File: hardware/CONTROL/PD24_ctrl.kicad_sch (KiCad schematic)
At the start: 11 parts, among them J1 Conn_01x12_Socket, J2 Conn_01x08_Socket, U2 STM32G031G8Ux, U5 INA228

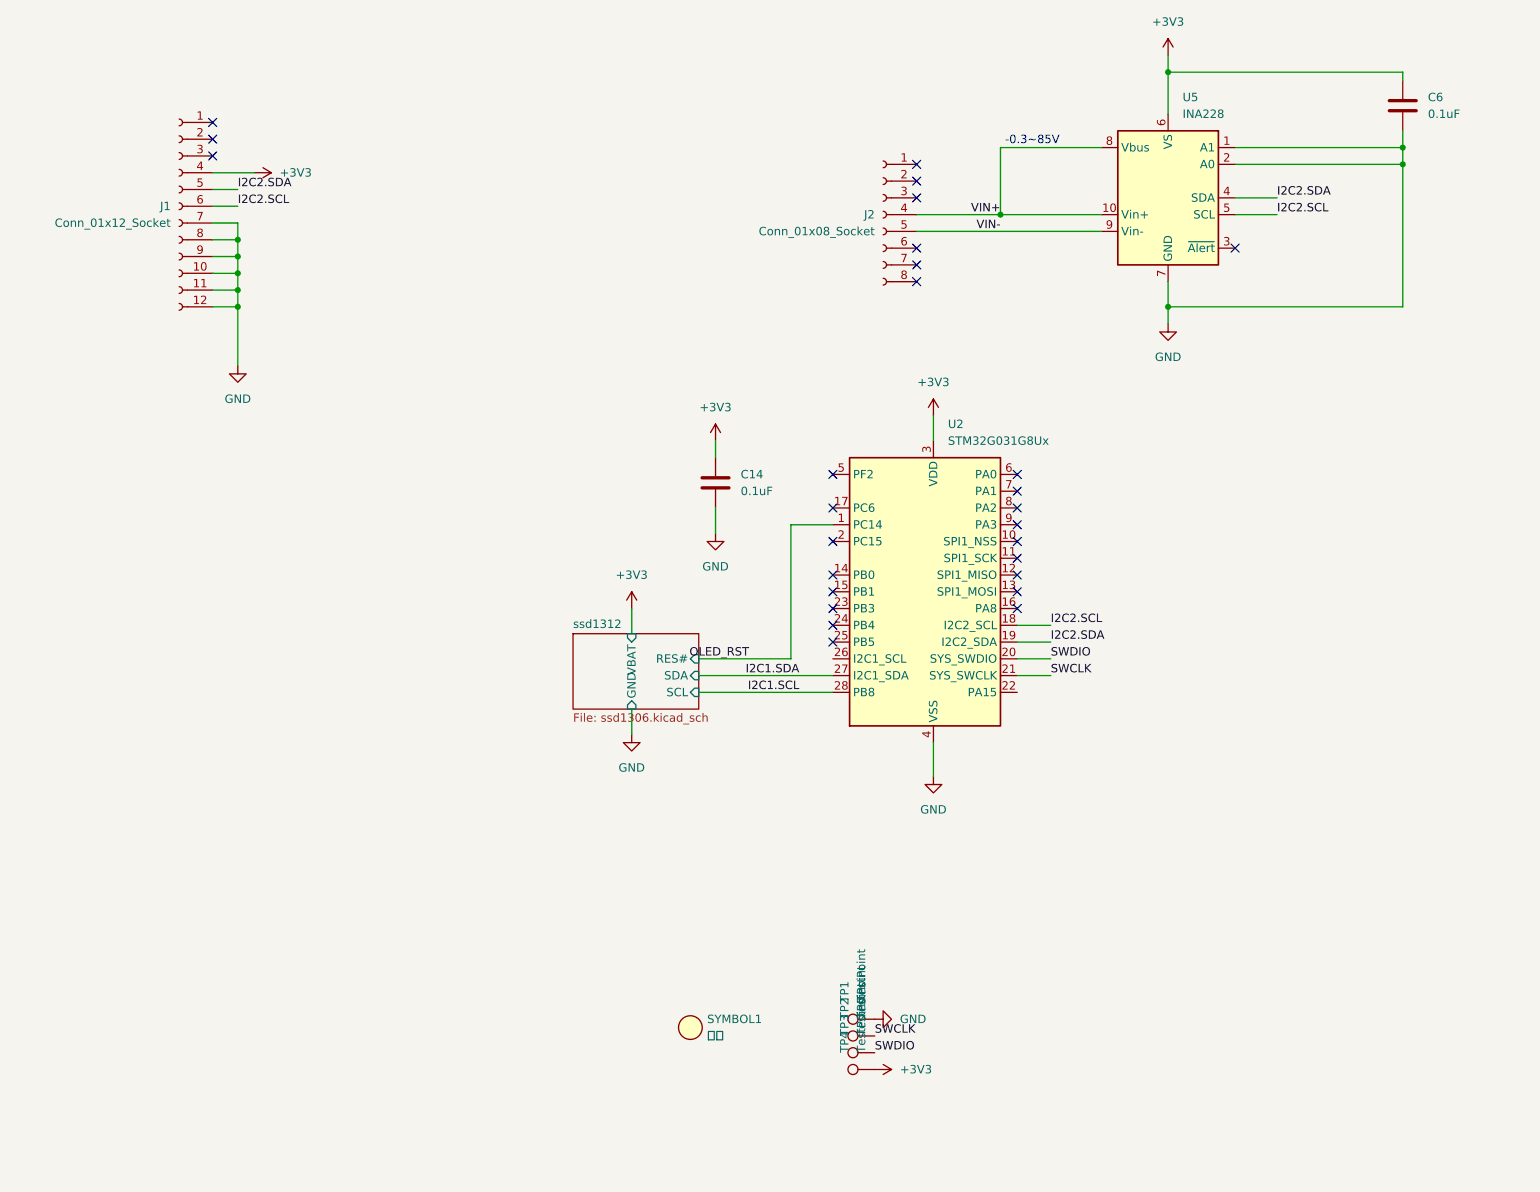
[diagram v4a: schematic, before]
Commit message: lis2dw12由于错误配置了cs脚，导致进入了spi模式，但电路设计上为iic的连接方式，无法读取方向，现在已经修正，但是代码设置成了固定方向。同步升压整流确实降低了不少发热，但是好像添加的ldo由于oled电流较大，带来的额外热量更多，之后可能还是考虑使用dcdc降压
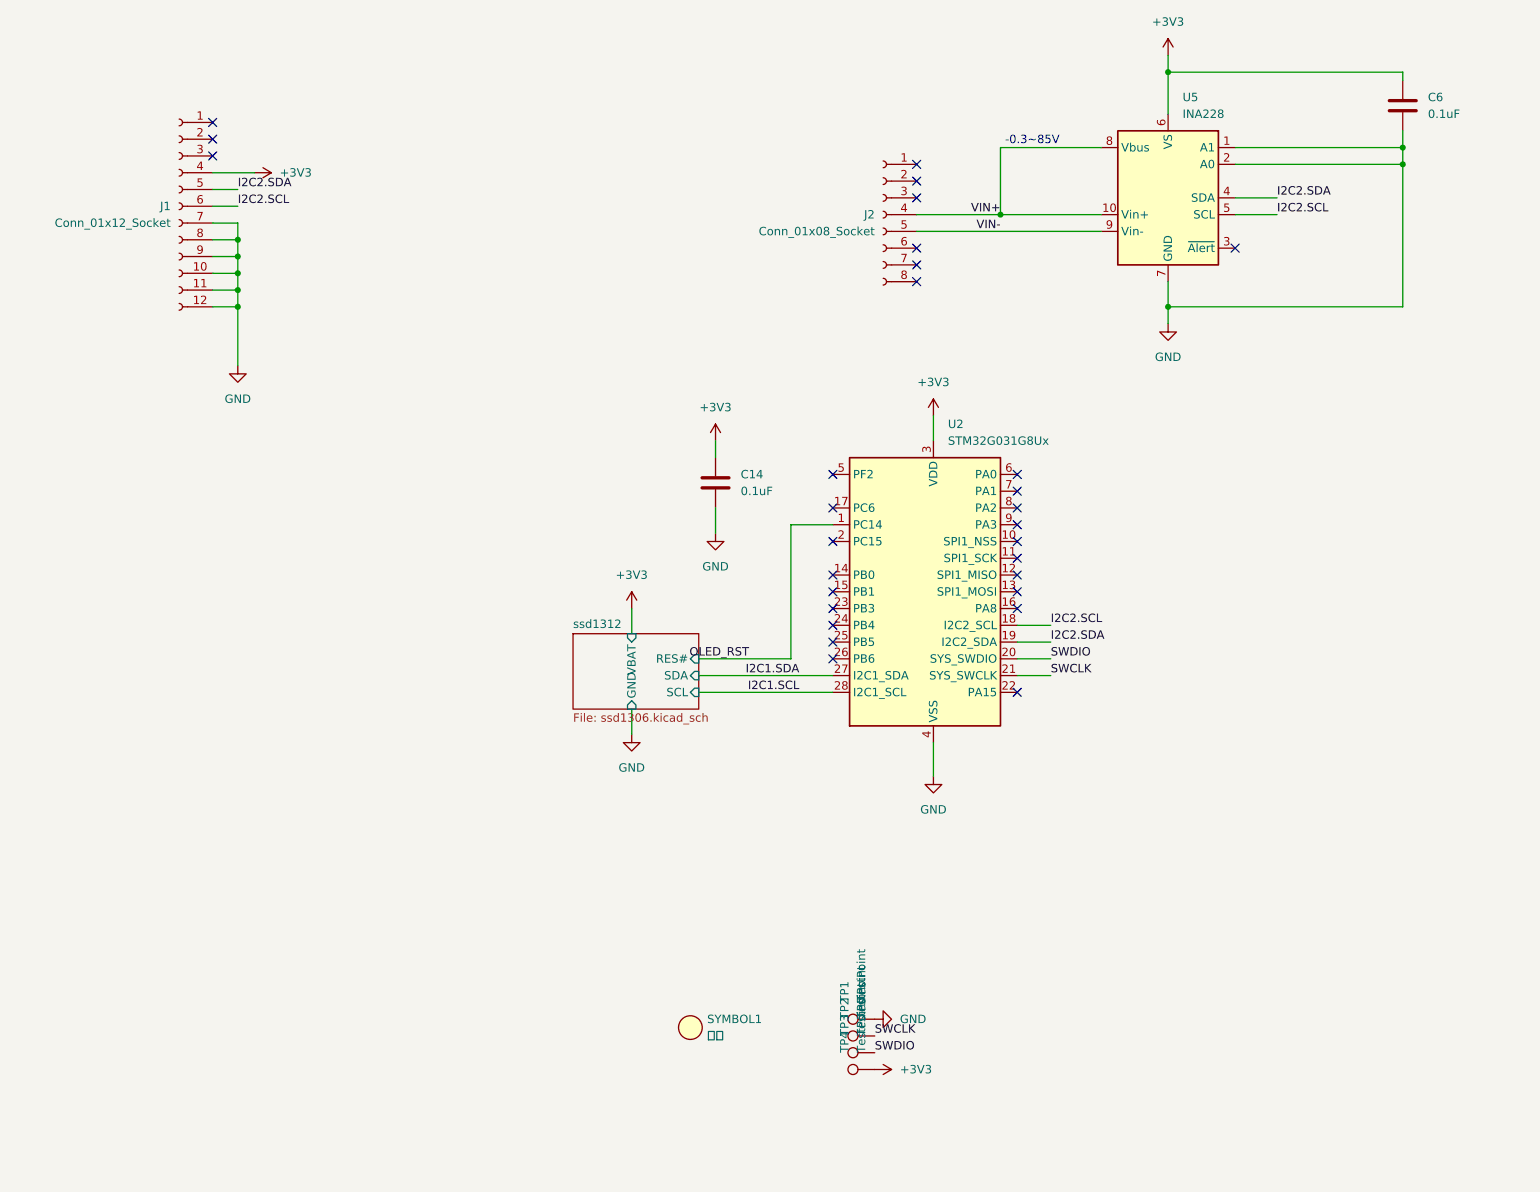
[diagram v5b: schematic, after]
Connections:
- no-connect marks 27 -> 29
